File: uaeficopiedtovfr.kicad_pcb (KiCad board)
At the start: 2 copper layers, 160 x 75.1 mm, 66 parts, among them J1 DTF13-12PB, J4 DTF13-12PB, J9 USB_C_Receptacle_USB2.0, M1 Module-power_12and5V-0.2, M2 Module-knock-0.2, M3 Module-vr-discrete-0.4, M4 Module-vr-max9924-0.1, M5 Module-wbo-0.5, M6 Module:mega-mcu100/0.2, M7 Module-wbo-0.5, P3 Pad, P4 Pad, Q1 ISL9V3040D3S, Q10 ZXMS6005SGTA, Q11 AO3400A, Q12 AO3400A, Q13 ZXMS6005SGTA, Q14 ZXMS6005SGTA, Q15 ZXMS6005SGTA, Q16 ZXMS6005SGTA, Q2 ISL9V3040D3S, Q3 ISL9V3040D3S, Q4 ISL9V3040D3S, Q7 ZXMS6005SGTA, Q8 ZXMS6005SGTA, Q9 ZXMS6005SGTA, U2 JDY-33

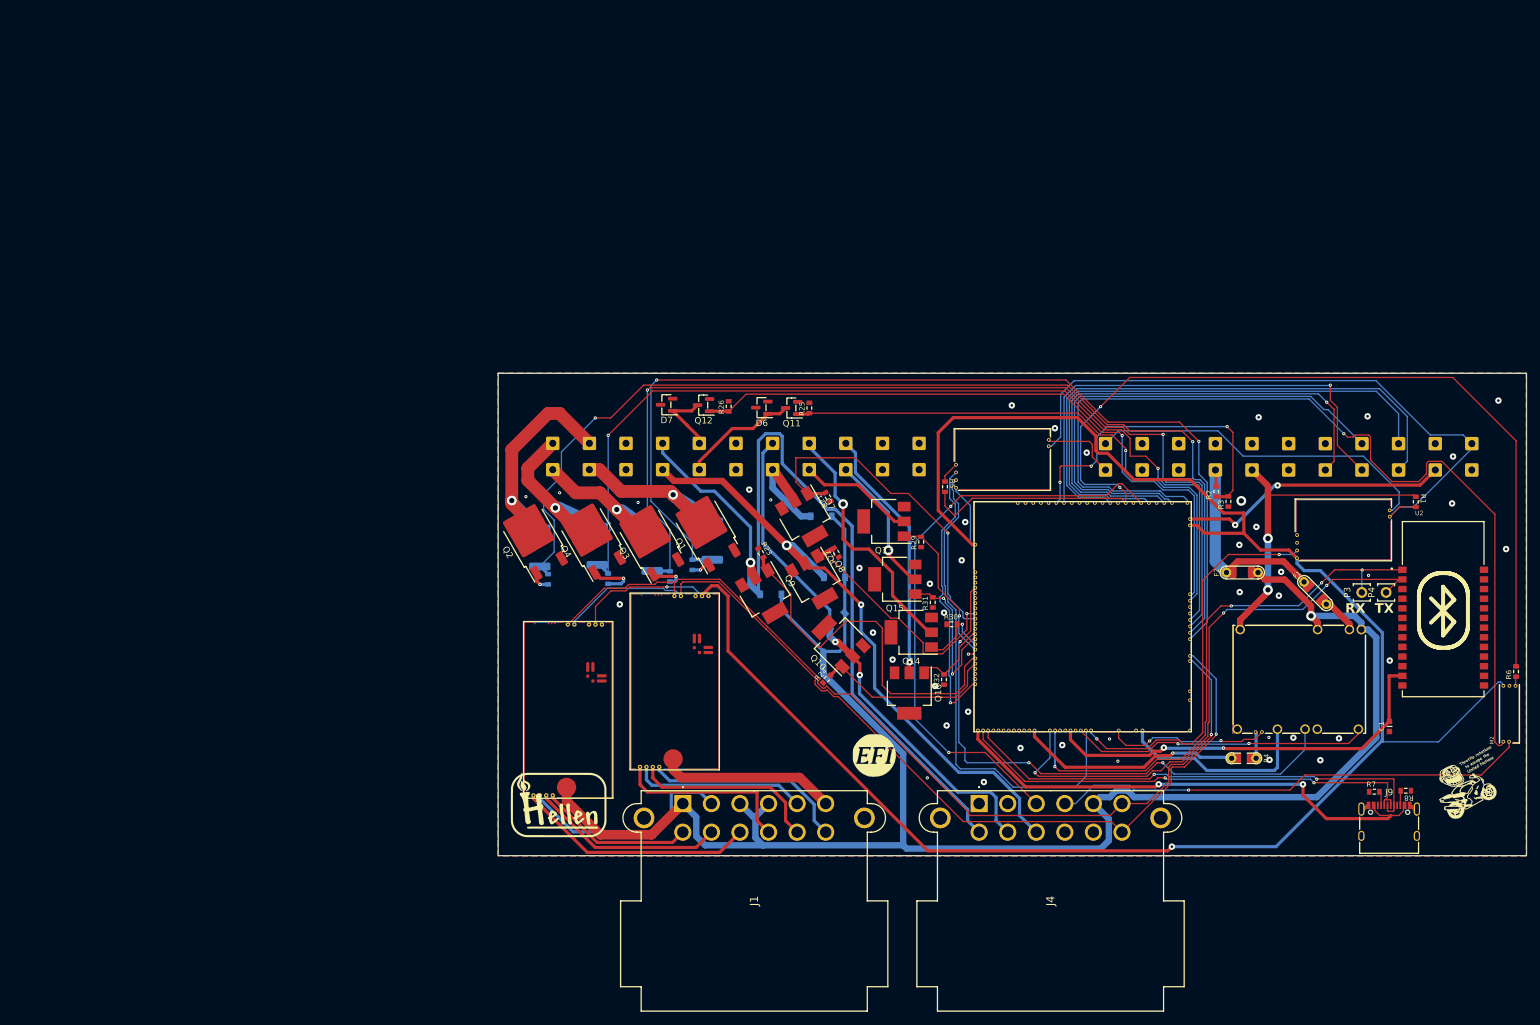
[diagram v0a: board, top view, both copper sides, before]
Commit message: Moved drill file again
last commit offset it 25mm in the opposite direction
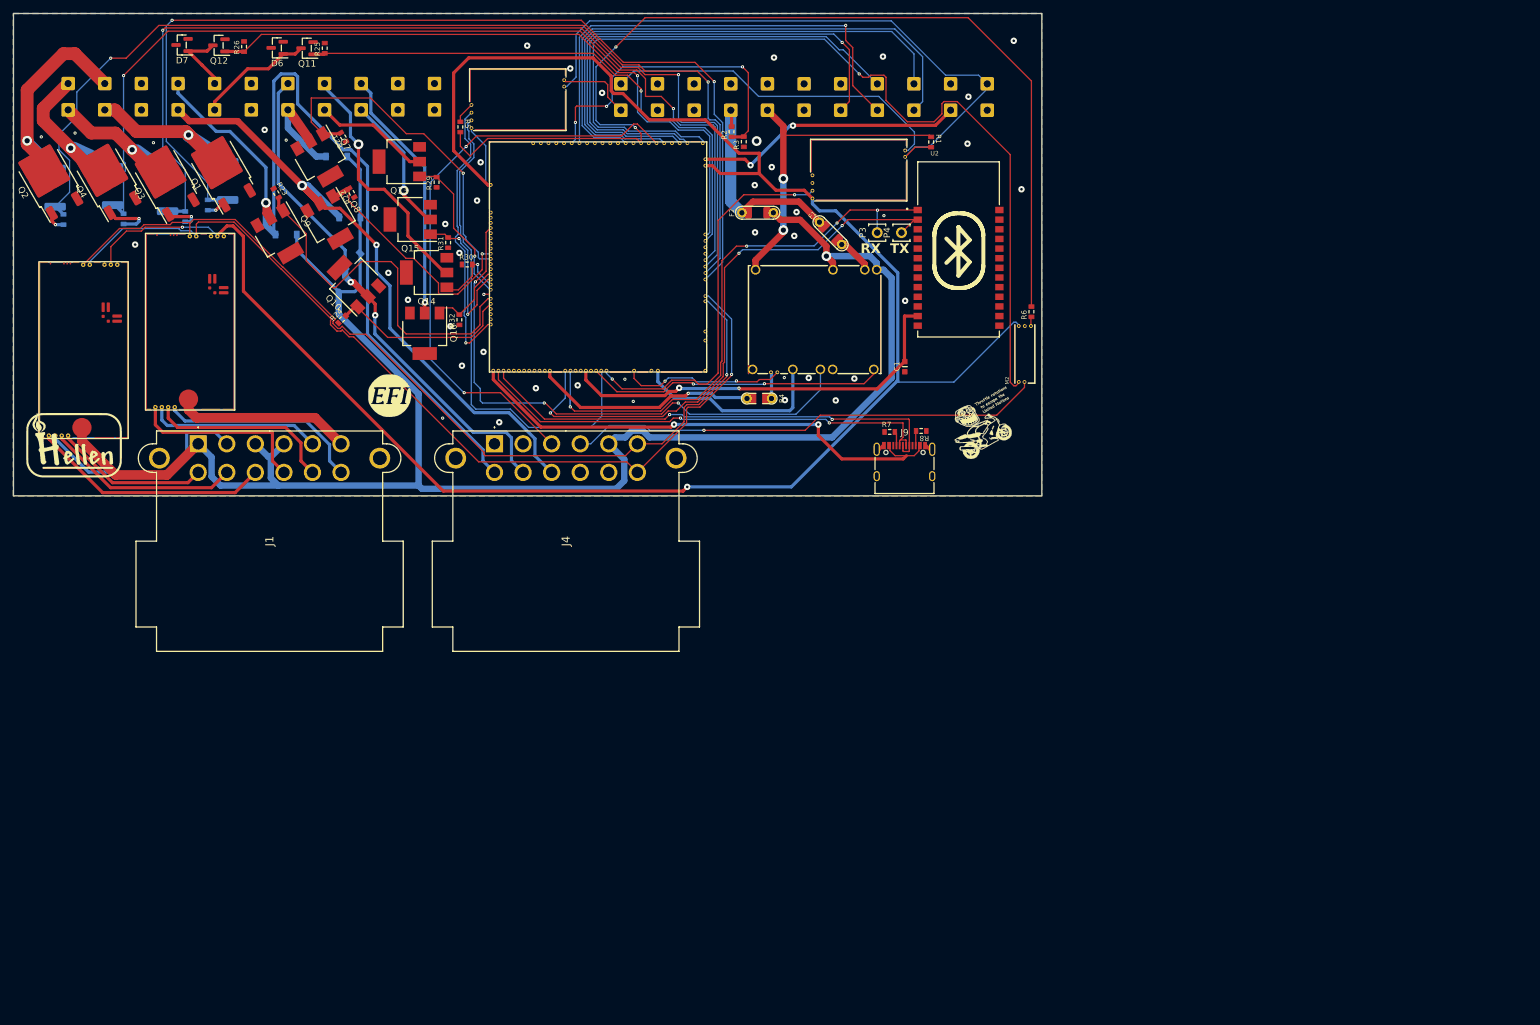
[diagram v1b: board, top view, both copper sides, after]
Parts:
- moved M6 93.9 mm to (109.8, 21.2)
- moved Q13 93.9 mm to (61.9, 24.4)
- moved Q14 93.9 mm to (66.1, 41.7)
- moved Q4 93.9 mm to (16.3, 26.9)
- moved Q8 93.9 mm to (51.1, 33.7)
- moved Q9 93.9 mm to (43.4, 35.9)
- moved R10 93.9 mm to (9.60, 33.4)
- moved R12 93.9 mm to (35.1, 27.4)
- moved R14 93.9 mm to (25.8, 29.2)
- moved R30 93.9 mm to (72.4, 40.4)
- moved R7 93.9 mm to (138.2, 66.5)
- moved R9 93.9 mm to (32.0, 31.2)
- moved text1 93.9 mm to (147.9, 70.6)
- moved C1 93.9 mm to (140.5, 56.3)
- moved D2 93.9 mm to (52.1, 23.6)
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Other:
- board size 160 x 75.1 mm -> 160 x 75 mm

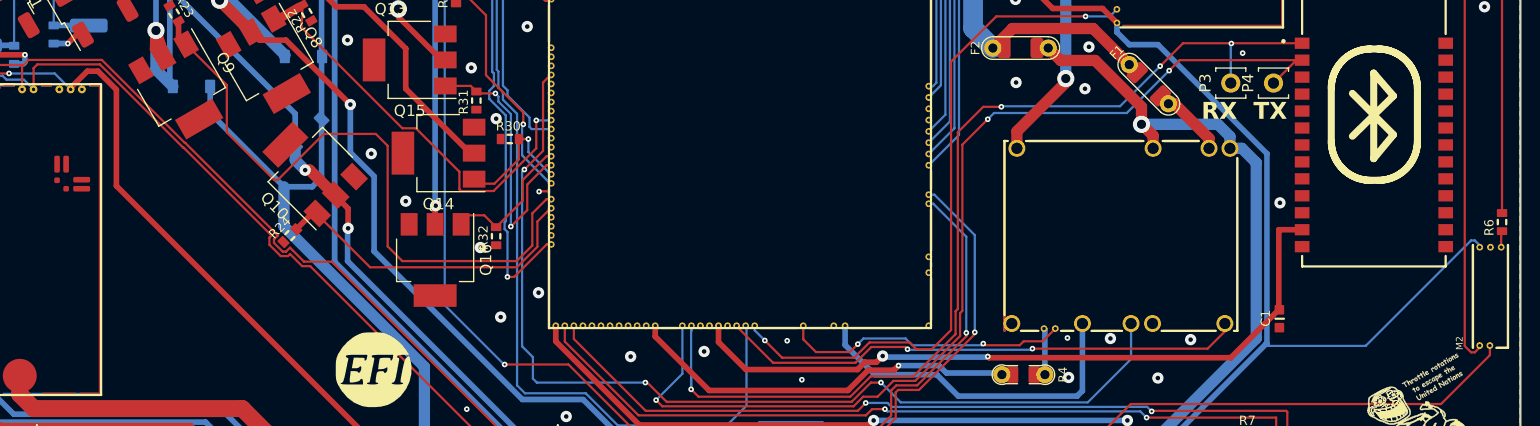
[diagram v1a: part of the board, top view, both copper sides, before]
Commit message: Added mounting holes
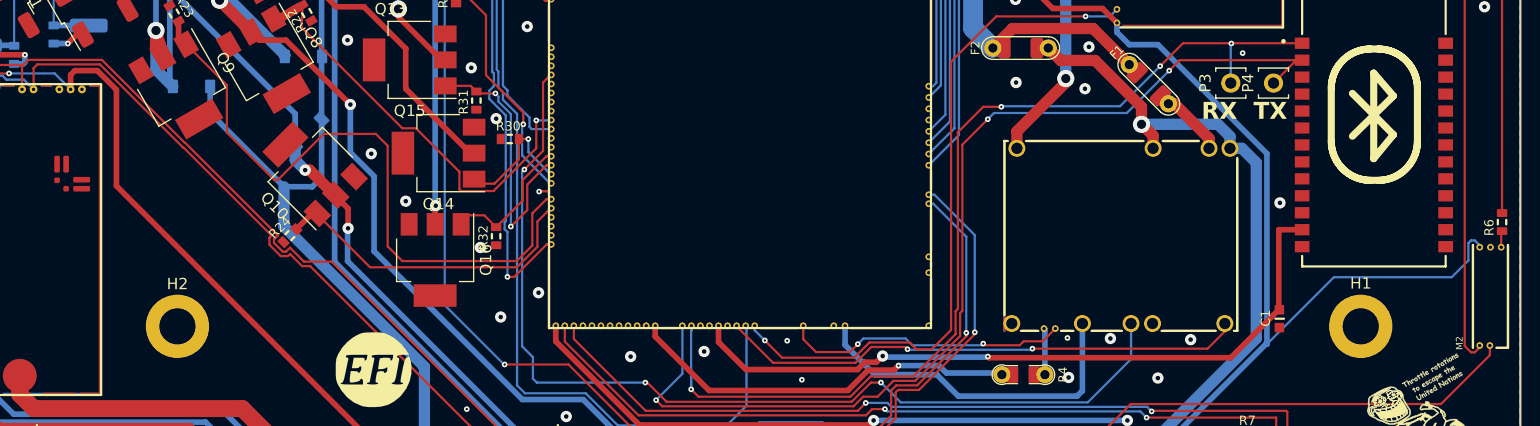
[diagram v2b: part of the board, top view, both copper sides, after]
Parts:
- added H1: MountingHole_Pad, MountingHole:MountingHole_3.2mm_M3_DIN965_Pad, F.Cu at (147.7, 57.0)
- added H2: MountingHole_Pad, MountingHole:MountingHole_3.2mm_M3_DIN965_Pad, F.Cu at (43.0, 57.0)
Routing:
- net +5VA: track 324.0 -> 325.5 mm
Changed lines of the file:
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@@
     )
   )
+  (footprint "MountingHole:MountingHole_3.2mm_M3_DIN965_Pad" (layer "F.Cu")
+    (at 43 57.05)
+    (descr "Mounting Hole 3.2mm, M3, DIN965")
+    (tags "mounting hole 3.2mm m3 din965")
+    (property "Sheetfile" "uaeficopiedtovfr.kicad_sch")
+    (property "Sheetname" "")
+    (property "ki_description" "Mounting Hole with connection")
+    (property "ki_keywords" "mounting hole")
+    (attr exclude_from_pos_files)
+    (fp_text reference "H2" (at 0 -3.8) (layer "F.SilkS")
+        (effects (font (size 1 1) (thickness 0.15)))
+    )
+    (fp_text value "MountingHole_Pad" (at 0 3.8) (layer "F.Fab")
+        (effects (font (size 1 1) (thickness 0.15)))
+    )
+    (fp_text user "${REFERENCE}" (at 0 0) (layer "F.Fab")
+        (effects (font (size 1 1) (thickness 0.15)))
+    )
+    (fp_circle (center 0 0) (end 2.8 0)
+      (stroke (width 0.15) (type solid)) (fill none) (layer "Cmts.User"))
+    (fp_circle (center 0 0) (end 3.05 0)
+      (stroke (width 0.05) (type solid)) (fill none) (layer "F.CrtYd"))
+    (pad "1" thru_hole circle (at 0 -0.05) (size 5.6 5.6) (drill 3.2) (layers "*.Cu" "*.Mask")
+      (net 1 "GND") (pinfunction "1") (pintype "input"))
+  )
   (footprint "Package_TO_SOT_SMD:SOT-223" (layer "F.Cu")
     (at 51.1 33.675 -60)
@@
     )
   )
+  (footprint "MountingHole:MountingHole_3.2mm_M3_DIN965_Pad" (layer "F.Cu")
+    (at 147.7 57)
+    (descr "Mounting Hole 3.2mm, M3, DIN965")
+    (tags "mounting hole 3.2mm m3 din965")
+    (property "Sheetfile" "uaeficopiedtovfr.kicad_sch")
+    (property "Sheetname" "")
+    (property "ki_description" "Mounting Hole with connection")
+    (property "ki_keywords" "mounting hole")
+    (attr exclude_from_pos_files)
+    (fp_text reference "H1" (at 0 -3.8) (layer "F.SilkS")
+        (effects (font (size 1 1) (thickness 0.15)))
+    )
+    (fp_text value "MountingHole_Pad" (at 0 3.8) (layer "F.Fab") hide
+        (effects (font (size 1 1) (thickness 0.15)))
+    )
+    (fp_text user "${REFERENCE}" (at 0 0) (layer "F.Fab")
+        (effects (font (size 1 1) (thickness 0.15)))
+    )
+    (fp_circle (center 0 0) (end 2.8 0)
+      (stroke (width 0.15) (type solid)) (fill none) (layer "Cmts.User"))
+    (fp_circle (center 0 0) (end 3.05 0)
+      (stroke (width 0.05) (type solid)) (fill none) (layer "F.CrtYd"))
+    (pad "1" thru_hole circle (at 0 0) (size 5.6 5.6) (drill 3.2) (layers "*.Cu" "*.Mask")
+      (net 1 "GND") (pinfunction "1") (pintype "input"))
+  )
   (footprint "Package_TO_SOT_SMD:TO-252-2" (layer "F.Cu")
     (at 25.346811 27.129285 120)
@@
   (segment (start 105.3995 59.6255) (end 105.499 59.725) (width 0.5) (layer "B.Cu") (net 36))
   (segment (start 19.4 35.225) (end 21.713826 35.225) (width 0.2) (layer "F.Cu") (net 37))
-  (segment (start 33.55 35.902429) (end 33.55 36.0338) (width 0.5) (layer "F.Cu") (net 37))
   (segment (start 91.972182 8.275) (end 94.825 11.127818) (width 0.5) (layer "F.Cu") (net 37))
+  (segment (start 33.55 34.75) (end 33.55 36.0338) (width 0.5) (layer "F.Cu") (net 37))
   (segment (start 70.3 10.625) (end 72.65 8.275) (width 0.5) (layer "F.Cu") (net 37))
   (segment (start 124.85 28.875) (end 126.125 30.15) (width 0.5) (layer "F.Cu") (net 37))
@@
   (segment (start 16.975 40.4588) (end 16.975 37.65) (width 0.2) (layer "F.Cu") (net 37))
   (segment (start 21.713826 35.225) (end 22.313826 34.625) (width 0.2) (layer "F.Cu") (net 37))
+  (segment (start 33.925 34.375) (end 33.55 34.75) (width 0.5) (layer "F.Cu") (net 37))
   (segment (start 117.844609 23.119609) (end 117.844609 26.275) (width 0.5) (layer "F.Cu") (net 37))
-  (segment (start 37.6 44.575) (end 37.6 36.057222) (width 0.5) (layer "F.Cu") (net 37))
   (segment (start 16.975 37.65) (end 19.4 35.225) (width 0.2) (layer "F.Cu") (net 37))
+  (segment (start 68.7 75.675) (end 37.6 44.575) (width 0.5) (layer "F.Cu") (net 37))
+  (segment (start 106 75.675) (end 68.7 75.675) (width 0.5) (layer "F.Cu") (net 37))
   (segment (start 76.075005 28.049995) (end 75.624995 28.049995) (width 0.5) (layer "F.Cu") (net 37))
   (segment (start 75.624995 28.049995) (end 70.3 22.725) (width 0.5) (layer "F.Cu") (net 37))
   (segment (start 109.494609 17.925) (end 114.689218 23.119609) (width 0.5) (layer "F.Cu") (net 37))
-  (segment (start 68.7 75.675) (end 37.6 44.575) (width 0.5) (layer "F.Cu") (net 37))
   (segment (start 114.689218 23.119609) (end 117.844609 23.119609) (width 0.5) (layer "F.Cu") (net 37))
+  (segment (start 35.917777 34.375) (end 33.925 34.375) (width 0.5) (layer "F.Cu") (net 37))
   (segment (start 22.313826 34.625) (end 28.1 34.625) (width 0.2) (layer "F.Cu") (net 37))
-  (segment (start 35.967778 34.425) (end 35.027429 34.425) (width 0.5) (layer "F.Cu") (net 37))
-  (segment (start 37.6 36.057222) (end 35.967778 34.425) (width 0.5) (layer "F.Cu") (net 37))
-  (segment (start 106.65 75.025) (end 106 75.675) (width 0.5) (layer "F.Cu") (net 37))
   (segment (start 72.65 8.275) (end 91.972182 8.275) (width 0.5) (layer "F.Cu") (net 37))
-  (segment (start 35.027429 34.425) (end 33.55 35.902429) (width 0.5) (layer "F.Cu") (net 37))
   (segment (start 94.825 13.414949) (end 95.235051 13.825) (width 0.5) (layer "F.Cu") (net 37))
-  (segment (start 106 75.675) (end 68.7 75.675) (width 0.5) (layer "F.Cu") (net 37))
   (segment (start 94.825 11.127818) (end 94.825 13.414949) (width 0.5) (layer "F.Cu") (net 37))
   (segment (start 109.475005 25.049995) (end 110.55 25.049995) (width 0.5) (layer "F.Cu") (net 37))
+  (segment (start 106.65 75.025) (end 106 75.675) (width 0.5) (layer "F.Cu") (net 37))
   (segment (start 95.235051 13.825) (end 96.65 13.825) (width 0.5) (layer "F.Cu") (net 37))
   (segment (start 96.65 13.825) (end 100.75 17.925) (width 0.5) (layer "F.Cu") (net 37))
   (segment (start 100.75 17.925) (end 109.494609 17.925) (width 0.5) (layer "F.Cu") (net 37))
+  (segment (start 37.6 44.575) (end 37.6 36.057223) (width 0.5) (layer "F.Cu") (net 37))
   (segment (start 111.775005 26.275) (end 110.55 25.049995) (width 0.5) (layer "F.Cu") (net 37))
   (segment (start 120.444609 28.875) (end 124.85 28.875) (width 0.5) (layer "F.Cu") (net 37))
   (segment (start 28.1 34.625) (end 28 34.625) (width 0.2) (layer "F.Cu") (net 37))
+  (segment (start 37.6 36.057223) (end 35.917777 34.375) (width 0.5) (layer "F.Cu") (net 37))
   (via (at 28.1 34.625) (size 0.5) (drill 0.2) (layers "F.Cu" "B.Cu") (net 37))
   (via (at 106.65 75.025) (size 1) (drill 0.4) (layers "F.Cu" "B.Cu") (net 37))
-  (segment (start 158.225002 49.834315) (end 158.225002 50) (width 0.2) (layer "B.Cu") (net 37))
   (segment (start 28.1 34.625) (end 32.1412 34.625) (width 0.2) (layer "B.Cu") (net 37))
+  (segment (start 157.225002 49.634315) (end 157.459317 49.4) (width 0.2) (layer "B.Cu") (net 37))
+  (segment (start 157.790687 49.4) (end 158.225002 49.834315) (width 0.2) (layer "B.Cu") (net 37))
   (segment (start 73.075 19.2) (end 73.075 19.725) (width 0.2) (layer "B.Cu") (net 37))
   (segment (start 129.75 32.075) (end 127.225 32.075) (width 0.5) (layer "B.Cu") (net 37))
   (segment (start 126.125 30.975) (end 126.125 30.15) (width 0.5) (layer "B.Cu") (net 37))
   (segment (start 75.3 27.825) (end 75.524995 28.049995) (width 0.2) (layer "B.Cu") (net 37))
-  (segment (start 157.790687 49.4) (end 158.225002 49.834315) (width 0.2) (layer "B.Cu") (net 37))
+  (segment (start 157.459317 49.4) (end 157.790687 49.4) (width 0.2) (layer "B.Cu") (net 37))
   (segment (start 122.85 75.025) (end 106.65 75.025) (width 0.5) (layer "B.Cu") (net 37))
-  (segment (start 148.134317 58.725) (end 157.459317 49.4) (width 0.2) (layer "B.Cu") (net 37))
+  (segment (start 157.225002 51.174998) (end 157.225002 49.634315) (width 0.2) (layer "B.Cu") (net 37))
   (segment (start 139.4 41.725) (end 129.75 32.075) (width 0.5) (layer "B.Cu") (net 37))
+  (segment (start 155.75 52.65) (end 157.225002 51.174998) (width 0.2) (layer "B.Cu") (net 37))
   (segment (start 73.075 19.725) (end 75.3 21.95) (width 0.2) (layer "B.Cu") (net 37))
-  (segment (start 157.459317 49.4) (end 157.790687 49.4) (width 0.2) (layer "B.Cu") (net 37))
+  (segment (start 139.4 58.575) (end 145.325 52.65) (width 0.2) (layer "B.Cu") (net 37))
+  (segment (start 158.225002 49.834315) (end 158.225002 50) (width 0.2) (layer "B.Cu") (net 37))
   (segment (start 75.3 21.95) (end 75.3 27.825) (width 0.2) (layer "B.Cu") (net 37))
+  (segment (start 145.325 52.65) (end 155.75 52.65) (width 0.2) (layer "B.Cu") (net 37))
   (segment (start 32.1412 34.625) (end 33.55 36.0338) (width 0.2) (layer "B.Cu") (net 37))
   (segment (start 139.3 58.575) (end 122.85 75.025) (width 0.5) (layer "B.Cu") (net 37))
   (segment (start 139.4 58.575) (end 139.3 58.575) (width 0.5) (layer "B.Cu") (net 37))
-  (segment (start 148.134317 58.725) (end 139.55 58.725) (width 0.2) (layer "B.Cu") (net 37))
   (segment (start 139.4 58.575) (end 139.4 41.725) (width 0.5) (layer "B.Cu") (net 37))
   (segment (start 127.225 32.075) (end 126.125 30.975) (width 0.5) (layer "B.Cu") (net 37))
-  (segment (start 139.55 58.725) (end 139.4 58.575) (width 0.2) (layer "B.Cu") (net 37))
   (segment (start 75.524995 28.049995) (end 76.075005 28.049995) (width 0.2) (layer "B.Cu") (net 37))
   (segment (start 95.701491 60.225) (end 92.475005 56.998514) (width 0.2) (layer "F.Cu") (net 38))
